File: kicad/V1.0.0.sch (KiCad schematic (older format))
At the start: 21 parts, among them IC1 OPA2134P

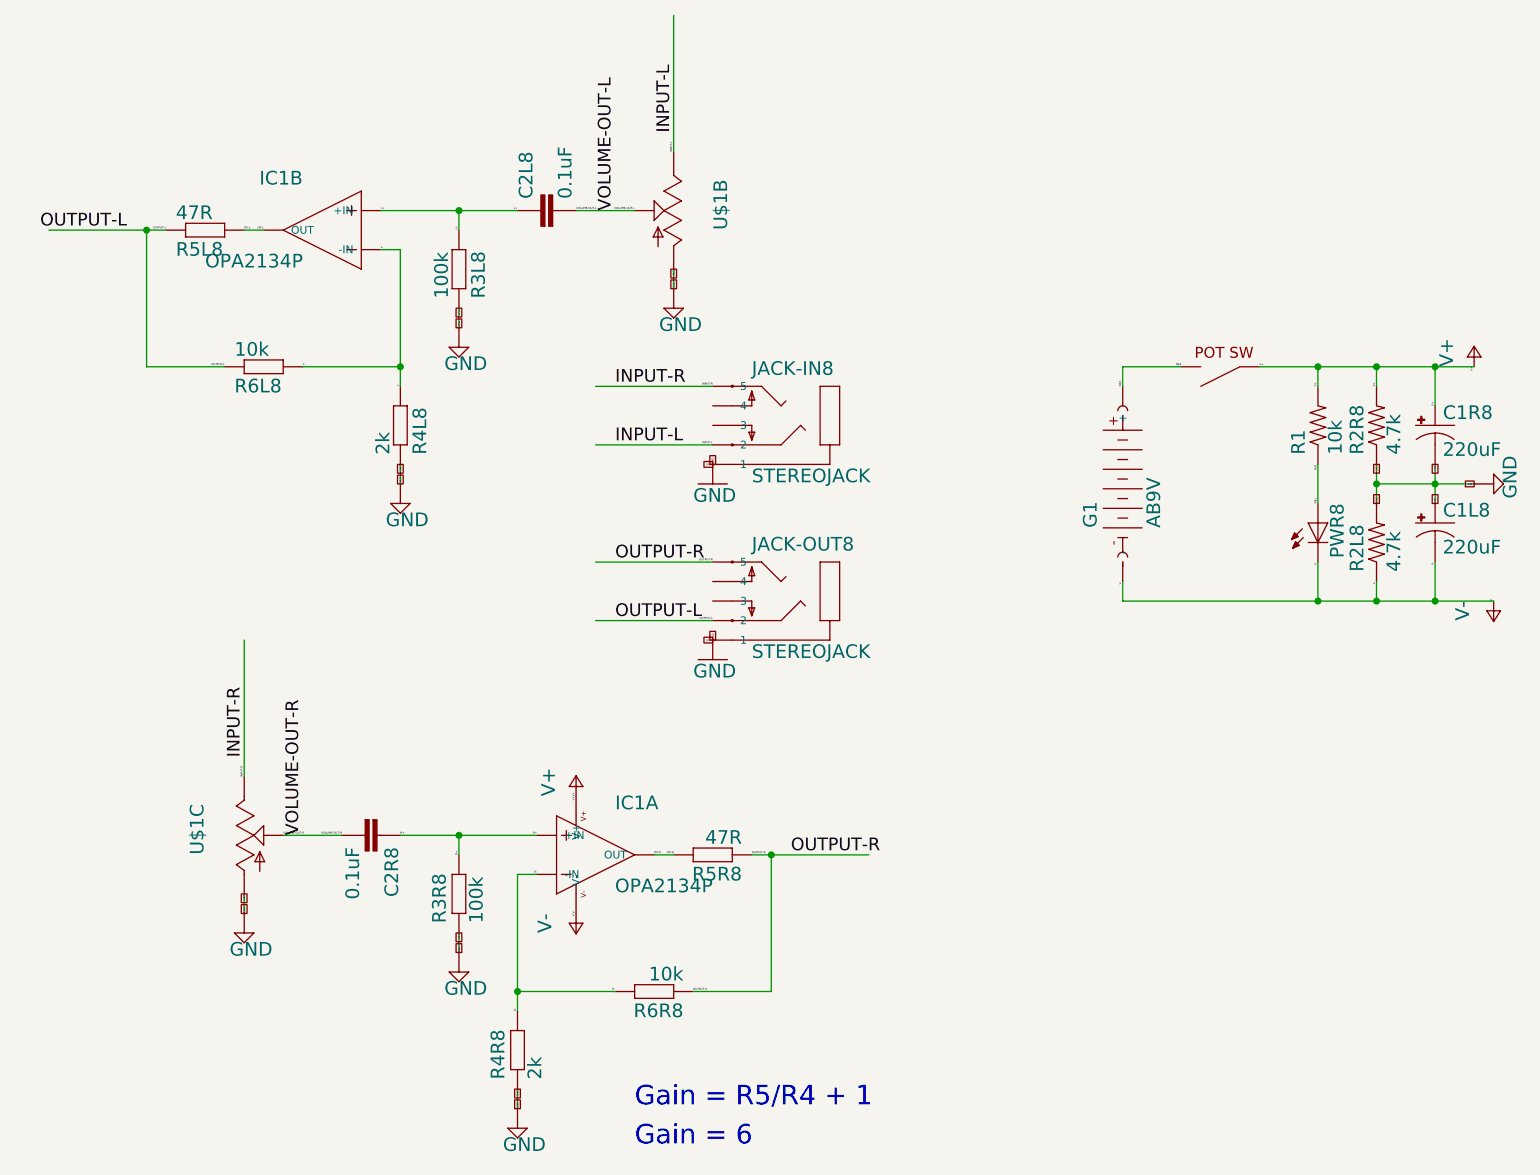
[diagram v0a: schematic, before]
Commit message: Modified slightly to fix some ERC issues
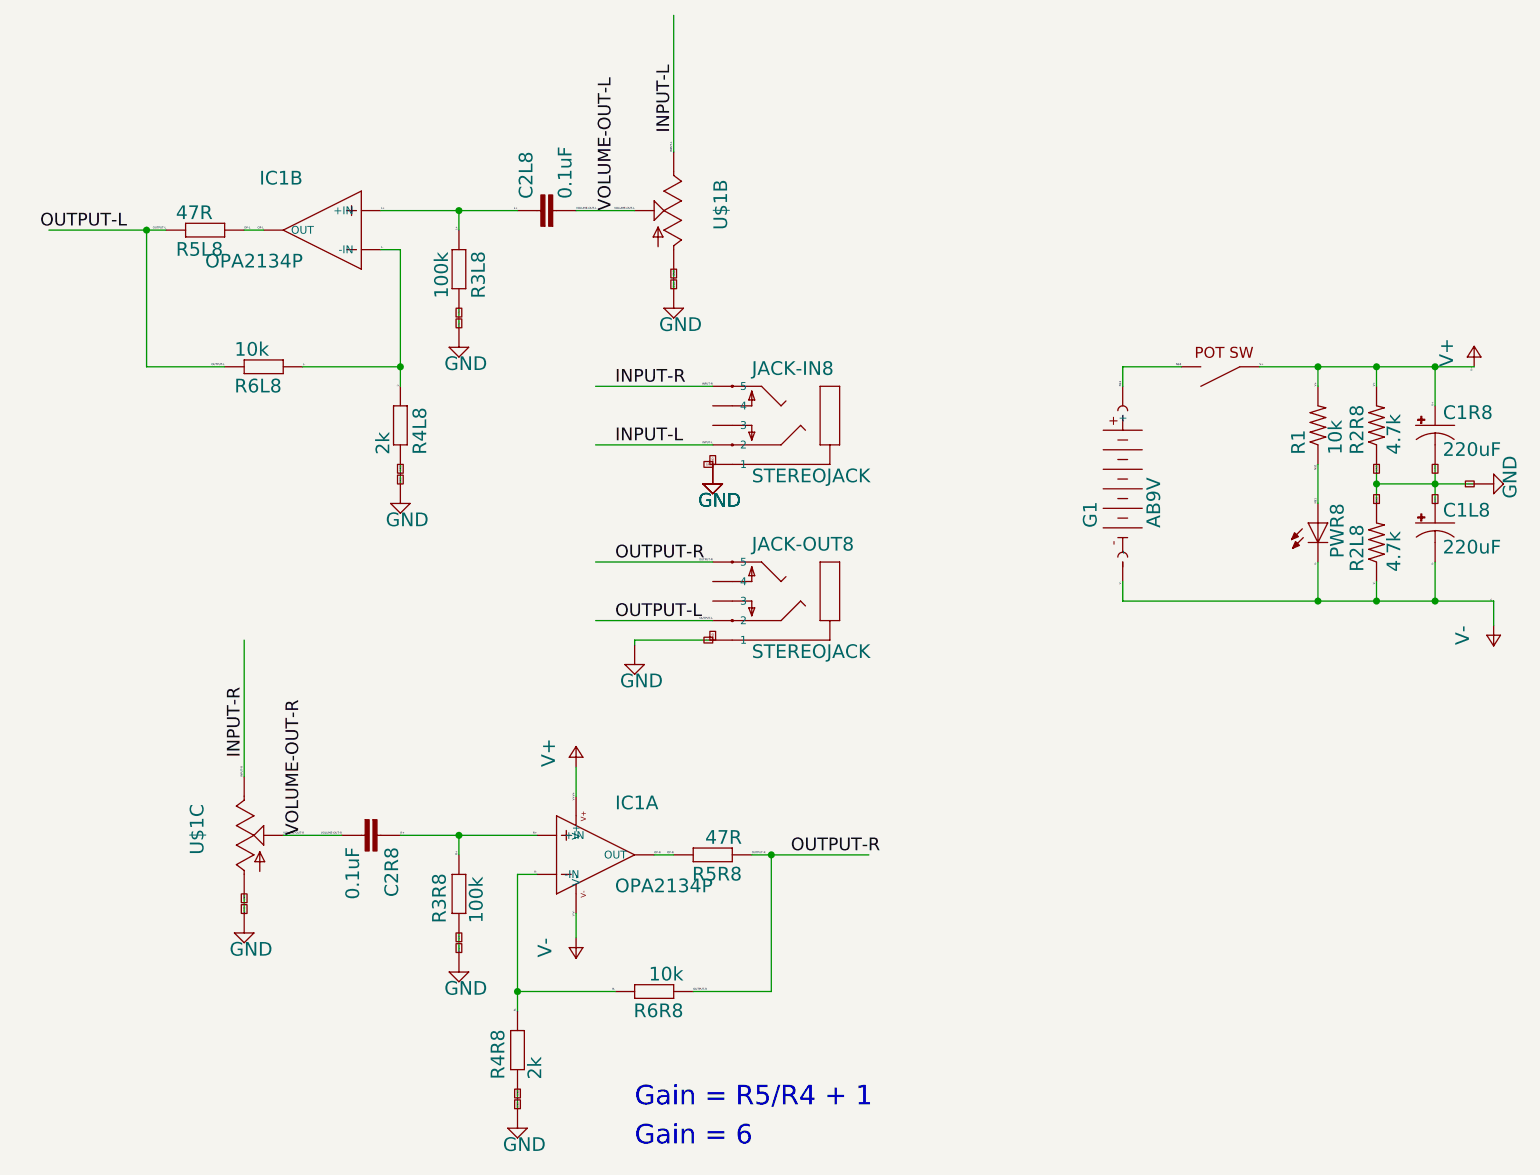
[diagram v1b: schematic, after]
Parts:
- C2L8, C2R8: footprint CAPACITOR-WIMA_C5B5 -> V1.0.1:CAPACITOR-WIMA_C5B5
- G1: footprint BATTERY_AB9V -> V1.0.1:BATTERY_AB9V
- IC1: footprint AKAFUGU_DIL-8 -> V1.0.1:AKAFUGU_DIL-8
- JACK-IN8, JACK-OUT8: footprint AKAFUGU_STX3100 -> V1.0.1:AKAFUGU_STX3100
- PWR8: value (none) -> ~
- R3L8, R3R8, R4L8, R4R8, R5L8, R5R8, R6L8, R6R8: footprint RESISTOR_0207_2V -> V1.0.1:RESISTOR_0207_2V
- U$1: value (none) -> ~; footprint AUDIO-POTS_ALPS_RK0971221Z0X -> V1.0.1:AUDIO-POTS_ALPS_RK0971221Z0X
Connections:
- wire segments 62 -> 52
